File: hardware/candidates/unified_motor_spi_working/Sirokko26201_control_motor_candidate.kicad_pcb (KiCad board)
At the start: 2 copper layers, 180 x 170 mm, 112 parts, among them J1 DEVKITC1_J1, J10 TC_K_EXHAUST_T+_T-, J102 MOTOR_24V_HIGH_SPEED; 125W_HE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, J11 TC_K_AIR_T+_T-, J12 ROOM_DS18B20_HARNESS, J13 24V_LOGIC_INPUT_ONLY__DRAFT_N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, J22 PANEL_DRY_CONTACTS_3V3, J23 LOCAL_BUTTONS_3V3__SET_UP_DOW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, J24 RESET_HW_SPDT_BBM_3V3, J25 THERMAL_AND_HW_ENABLE_3V3_ONLY, J26 TFT_GMT020-02-7P_ST7789V_7P_S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, J3 DEVKITC1_J3, Q101 IRFB4110PBF (100V; RDS(on) @ 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, U1 TPS3431SDRBR, U10 MAX31856MUD+, U101 LM5013DDAR, U2 SN74HCS74D, U3 SN74HCS14D, U4 SN74HCS30D, U5 SN74HCS30D, U6 SN74HCS11D, U7 TPS3839G33DBZR, U8 SN74LVC1G14DBVR, U9 MAX31856MUD+, U9001 LTC7001IMSE#PBF; MSOP-10 EP, U9002 INA240A1ID, U9003 LMV331M5X/NOPB, U9004 SN74LVC1G32DBVR, U9005 SN74LVC1G08DBVR, U9006 SN74LVC1G08DBVR, U9007 LM317HVT/NOPB TO-220; TJ 0…12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

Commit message: hardware: WIP continue unified TFT routing 215-55
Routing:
- net /TFT_DC: track 0.00 -> 108.4 mm
- net /TFT_CS: track 0.00 -> 105.8 mm, vias 0 -> 1
- net /+3V3: track 72.6 -> 96.4 mm, vias 1 -> 2
- net /TFT_RESET_N: track 0.00 -> 8.82 mm, vias 0 -> 1
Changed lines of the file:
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@@
+	)
+	(segment
+		(start 21 74.975)
+		(end 24 74.975)
+		(width 0.4)
+		(layer "F.Cu")
+		(net "/+3V3")
 	)
 	(segment
@@
 	)
 	(segment
+		(start 24 74.975)
+		(end 24 87.7)
+		(width 0.4)
+		(layer "F.Cu")
+		(net "/+3V3")
+	)
+	(segment
 		(start 27.875 29.05)
 		(end 25 27.5)
@@
 	)
 	(via
+		(at 24 87.7)
+		(size 0.6)
+		(drill 0.3)
+		(layers "F.Cu" "B.Cu")
+		(net "/+3V3")
+	)
+	(via
 		(at 21.725 29.05)
 		(size 0.6)
@@
 		)
 		(filling no)
+		(net "/+3V3")
+	)
+	(segment
+		(start 24 87.7)
+		(end 16 87.7)
+		(width 0.4)
+		(layer "B.Cu")
 		(net "/+3V3")
 	)
@@
 	)
 	(segment
+		(start 19.5 76.625)
+		(end 21 76.625)
+		(width 0.25)
+		(layer "F.Cu")
+		(net "/TFT_CS")
+	)
+	(segment
+		(start 20 94)
+		(end 79.8 94)
+		(width 0.25)
+		(layer "F.Cu")
+		(net "/TFT_CS")
+	)
+	(segment
+		(start 20 77.625)
+		(end 20 94)
+		(width 0.25)
+		(layer "F.Cu")
+		(net "/TFT_CS")
+	)
+	(segment
+		(start 21 76.625)
+		(end 20 77.625)
+		(width 0.25)
+		(layer "F.Cu")
+		(net "/TFT_CS")
+	)
+	(segment
+		(start 16 75)
+		(end 19.5 75)
+		(width 0.25)
+		(layer "F.Cu")
+		(net "/TFT_CS")
+	)
+	(segment
+		(start 19.5 75)
+		(end 19.5 76.625)
+		(width 0.25)
+		(layer "F.Cu")
+		(net "/TFT_CS")
+	)
+	(segment
+		(start 79.8 94)
+		(end 79.8 75.64)
+		(width 0.25)
+		(layer "F.Cu")
+		(net "/TFT_CS")
+	)
+	(via
+		(at 79.8 75.64)
+		(size 0.6)
+		(drill 0.3)
+		(layers "F.Cu" "B.Cu")
+		(net "/TFT_CS")
+	)
+	(segment
+		(start 79.8 75.64)
+		(end 83 75.64)
+		(width 0.25)
+		(layer "B.Cu")
+		(net "/TFT_CS")
+	)
+	(segment
 		(start 120.825 68)
 		(end 125 68.825)
@@
 	)
 	(segment
+		(start 22.5 80.075)
+		(end 22.5 79.5)
+		(width 0.25)
+		(layer "F.Cu")
+		(net "/TFT_RESET_N")
+	)
+	(segment
+		(start 21 80.075)
+		(end 22.5 80.075)
+		(width 0.25)
+		(layer "F.Cu")
+		(net "/TFT_RESET_N")
+	)
+	(via
+		(at 22.5 79.5)
+		(size 0.6)
+		(drill 0.3)
+		(layers "F.Cu" "B.Cu")
+		(net "/TFT_RESET_N")
+	)
+	(segment
+		(start 18.42 80.08)
+		(end 16 80.08)
+		(width 0.25)
+		(layer "B.Cu")
+		(net "/TFT_RESET_N")
+	)
+	(segment
+		(start 22.5 79.5)
+		(end 19 79.5)
+		(width 0.25)
+		(layer "B.Cu")
+		(net "/TFT_RESET_N")
+	)
+	(segment
+		(start 19 79.5)
+		(end 18.42 80.08)
+		(width 0.25)
+		(layer "B.Cu")
+		(net "/TFT_RESET_N")
+	)
+	(segment
 		(start 63.5 26.5)
 		(end 59.725 26.5)
@@
 		(net "/TC_EXH_DRDY")
 	)
+	(segment
+		(start 18 96)
+		(end 81.5 96)
+		(width 0.25)
+		(layer "F.Cu")
+		(net "/TFT_DC")
+	)
+	(segment
+		(start 18 77.54)
+		(end 18 96)
+		(width 0.25)
+		(layer "F.Cu")
+		(net "/TFT_DC")
+	)
+	(segment
+		(start 81.5 73.1)
+		(end 83 73.1)
+		(width 0.25)
+		(layer "F.Cu")
+		(net "/TFT_DC")
+	)
+	(segment
+		(start 16 77.54)
+		(end 18 77.54)
+		(width 0.25)
+		(layer "F.Cu")
+		(net "/TFT_DC")
+	)
+	(segment
+		(start 81.5 96)
+		(end 81.5 73.1)
+		(width 0.25)
+		(layer "F.Cu")
+		(net "/TFT_DC")
+	)
 	(zone

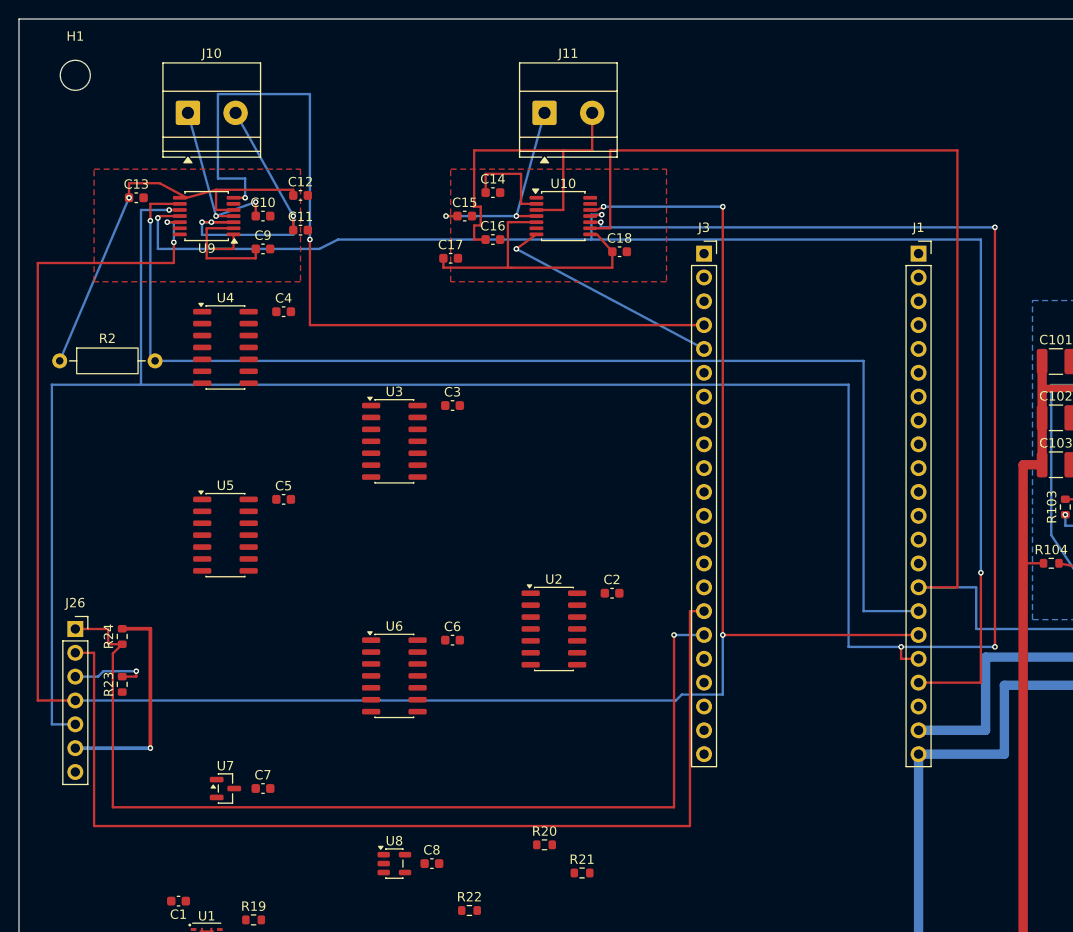
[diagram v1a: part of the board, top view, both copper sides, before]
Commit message: hardware: WIP route unified TFT power ground and EN 251-72
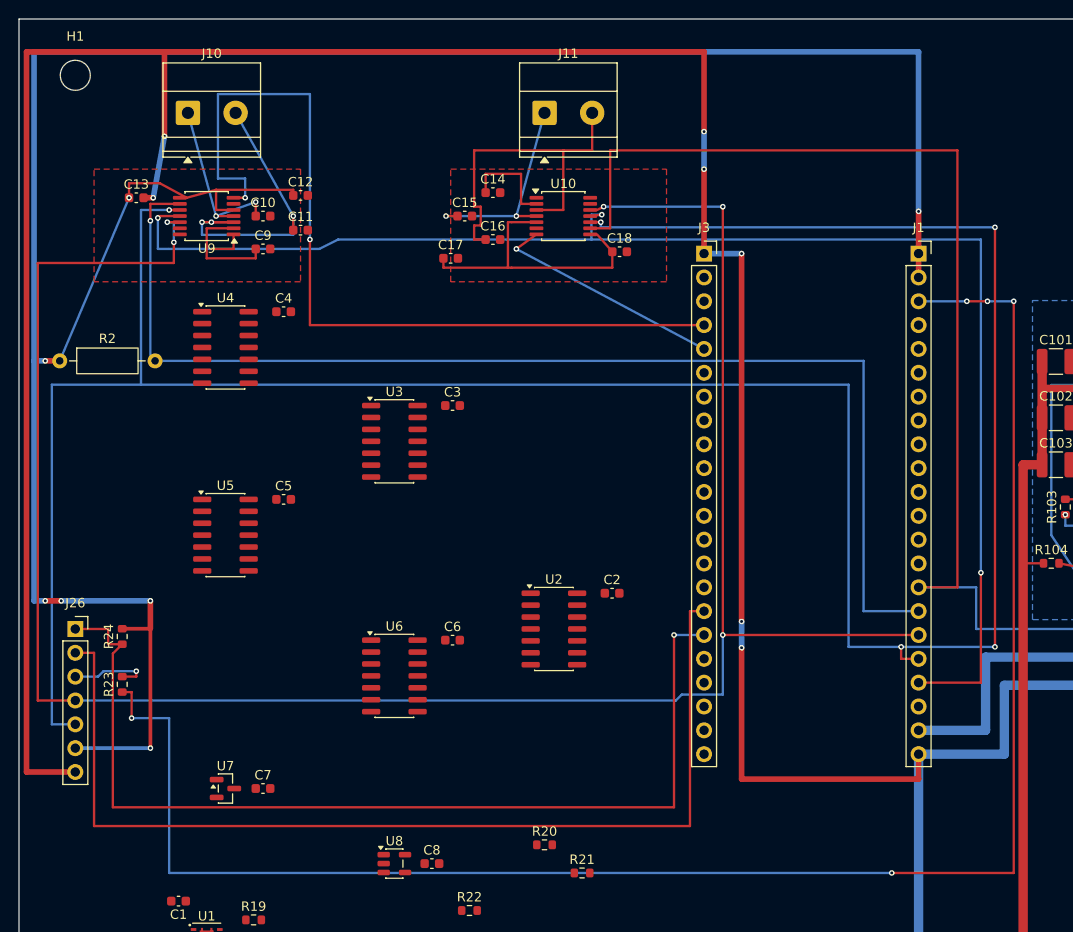
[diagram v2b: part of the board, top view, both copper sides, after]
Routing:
- net /GND: track 226.1 -> 500.0 mm, vias 9 -> 16
- net /+3V3: track 96.4 -> 291.3 mm, vias 2 -> 7
- net /EN_CHIP_PU: track 0.00 -> 185.3 mm, vias 0 -> 5

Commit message: hardware: WIP publish U4/U5 logic supply routing 283/72
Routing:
- net /+3V3: track 291.3 -> 385.4 mm
- net /GND: track 500.0 -> 571.2 mm
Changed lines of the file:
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@@
+	)
+	(segment
+		(start 36 61.19)
+		(end 36 65)
+		(width 0.4)
+		(layer "F.Cu")
+		(net "/+3V3")
+	)
+	(segment
+		(start 36 59)
+		(end 36 61.19)
+		(width 0.4)
+		(layer "F.Cu")
+		(net "/+3V3")
 	)
 	(segment
@@
 	)
 	(segment
+		(start 34.475 41.19)
+		(end 37.425 41.19)
+		(width 0.4)
+		(layer "F.Cu")
+		(net "/+3V3")
+	)
+	(segment
 		(start 62.1 31.65)
 		(end 62.1 36.5)
@@
 	)
 	(segment
+		(start 27 59)
+		(end 27 67.54)
+		(width 0.25)
+		(layer "F.Cu")
+		(net "/+3V3")
+	)
+	(segment
 		(start 31 30.35)
 		(end 31 28.2)
@@
 	)
 	(segment
+		(start 18 42.77)
+		(end 18 39)
+		(width 0.4)
+		(layer "F.Cu")
+		(net "/+3V3")
+	)
+	(segment
+		(start 34.475 63.73)
+		(end 36 63.73)
+		(width 0.25)
+		(layer "F.Cu")
+		(net "/+3V3")
+	)
+	(segment
+		(start 14.34 46.43)
+		(end 18 50.09)
+		(width 0.4)
+		(layer "F.Cu")
+		(net "/+3V3")
+	)
+	(segment
 		(start 55.225 36.5)
 		(end 55.225 35.5)
@@
 	)
 	(segment
+		(start 18 50.09)
+		(end 18 59)
+		(width 0.4)
+		(layer "F.Cu")
+		(net "/+3V3")
+	)
+	(segment
 		(start 31 28.2)
 		(end 39.225 28.2)
@@
 	)
 	(segment
+		(start 34.475 43.73)
+		(end 36 43.73)
+		(width 0.25)
+		(layer "F.Cu")
+		(net "/+3V3")
+	)
+	(segment
 		(start 73.225 36.5)
 		(end 73.225 34.8)
@@
 	)
 	(segment
+		(start 14.34 46.43)
+		(end 18 42.77)
+		(width 0.4)
+		(layer "F.Cu")
+		(net "/+3V3")
+	)
+	(segment
+		(start 27 67.54)
+		(end 29.525 67.54)
+		(width 0.25)
+		(layer "F.Cu")
+		(net "/+3V3")
+	)
+	(segment
 		(start 105.86 30.5)
 		(end 105.86 35)
@@
 	)
 	(segment
+		(start 36 41.19)
+		(end 36 45)
+		(width 0.4)
+		(layer "F.Cu")
+		(net "/+3V3")
+	)
+	(segment
+		(start 34.475 65)
+		(end 36 65)
+		(width 0.25)
+		(layer "F.Cu")
+		(net "/+3V3")
+	)
+	(segment
+		(start 34.475 61.19)
+		(end 37.425 61.19)
+		(width 0.4)
+		(layer "F.Cu")
+		(net "/+3V3")
+	)
+	(segment
 		(start 14.5 72)
 		(end 12.8 72)
@@
 	)
 	(segment
+		(start 36 39)
+		(end 36 41.19)
+		(width 0.4)
+		(layer "F.Cu")
+		(net "/+3V3")
+	)
+	(segment
+		(start 18 59)
+		(end 36 59)
+		(width 0.4)
+		(layer "F.Cu")
+		(net "/+3V3")
+	)
+	(segment
 		(start 64.4 31.65)
 		(end 62.5 31.65)
@@
 	)
 	(segment
+		(start 34.475 45)
+		(end 36 45)
+		(width 0.25)
+		(layer "F.Cu")
+		(net "/+3V3")
+	)
+	(segment
 		(start 62.5 36.5)
 		(end 73.225 36.5)
 		(width 0.25)
+		(layer "F.Cu")
+		(net "/+3V3")
+	)
+	(segment
+		(start 18 39)
+		(end 36 39)
+		(width 0.4)
 		(layer "F.Cu")
 		(net "/+3V3")
@@
 	)
 	(segment
+		(start 38.975 61.19)
+		(end 39.7 60.465)
+		(width 0.4)
+		(layer "F.Cu")
+		(net "/GND")
+	)
+	(segment
 		(start 10.8 13.5)
 		(end 83 13.5)
 		(width 0.6)
+		(layer "F.Cu")
+		(net "/GND")
+	)
+	(segment
+		(start 39.7 50.3)
+		(end 39.7 40.465)
+		(width 0.4)
+		(layer "F.Cu")
+		(net "/GND")
+	)
+	(segment
+		(start 29.525 48.81)
+		(end 28.2 48.81)
+		(width 0.4)
 		(layer "F.Cu")
 		(net "/GND")
@@
 	)
 	(segment
+		(start 28.2 70.3)
+		(end 39.7 70.3)
+		(width 0.4)
+		(layer "F.Cu")
+		(net "/GND")
+	)
+	(segment
 		(start 121.975 46.5)
 		(end 123.5 46.5)
@@
 	)
 	(segment
+		(start 39.7 38)
+		(end 36.775 35.075)
+		(width 0.4)
+		(layer "F.Cu")
+		(net "/GND")
+	)
+	(segment
 		(start 121.975 52.5)
 		(end 123.5 52.5)
@@
 	)
 	(segment
+		(start 28.2 68.81)
+		(end 28.2 70.3)
+		(width 0.4)
+		(layer "F.Cu")
+		(net "/GND")
+	)
+	(segment
+		(start 29.525 68.81)
+		(end 28.2 68.81)
+		(width 0.4)
+		(layer "F.Cu")
+		(net "/GND")
+	)
+	(segment
 		(start 168 43.525)
 		(end 173 43.525)
@@
 	)
 	(segment
+		(start 39.7 70.3)
+		(end 39.7 60.465)
+		(width 0.4)
+		(layer "F.Cu")
+		(net "/GND")
+	)
+	(segment
 		(start 121.975 57.5)
 		(end 123.5 57.5)
@@
 	)
 	(segment
+		(start 28.2 48.81)
+		(end 28.2 50.3)
+		(width 0.4)
+		(layer "F.Cu")
+		(net "/GND")
+	)
+	(segment
 		(start 125.3 48.095)
 		(end 128 48.095)
@@
 	)
 	(segment
+		(start 38.975 41.19)
+		(end 39.7 40.465)
+		(width 0.4)
+		(layer "F.Cu")
+		(net "/GND")
+	)
+	(segment
 		(start 16 90.24)
 		(end 10.8 90.24)
@@
 		(end 83 22)
 		(width 0.6)
+		(layer "F.Cu")
+		(net "/GND")
+	)
+	(segment
+		(start 39.7 60.465)
+		(end 39.7 50.3)
+		(width 0.4)
 		(layer "F.Cu")
 		(net "/GND")
@@
 	)
 	(segment
+		(start 28.2 50.3)
+		(end 39.7 50.3)
+		(width 0.4)
+		(layer "F.Cu")
+		(net "/GND")
+	)
+	(segment
 		(start 121.5 61.175)
 		(end 122.7 61.175)
@@
 		(layer "F.Cu")
 		(net "/GND")
+	)
+	(segment
+		(start 36.775 35.075)
+		(end 36.775 31)
+		(width 0.4)
+		(layer "F.Cu")
+		(net "/GND")
+	)
+	(segment
+		(start 39.7 40.465)
+		(end 39.7 38)
+		(width 0.4)
+		(layer "F.Cu")
+		(net "/GND")

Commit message: hardware: WIP publish U3/C3 supply 294/74 and RESET erratum
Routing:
- net /GND: track 571.2 -> 605.7 mm
- net /+3V3: track 385.4 -> 413.9 mm, vias 7 -> 9
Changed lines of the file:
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@@
+	)
+	(segment
+		(start 42 45)
+		(end 42 49)
+		(width 0.4)
+		(layer "F.Cu")
+		(net "/+3V3")
 	)
 	(segment
@@
 	)
 	(segment
+		(start 55.425 49)
+		(end 55.425 51.19)
+		(width 0.4)
+		(layer "F.Cu")
+		(net "/+3V3")
+	)
+	(segment
+		(start 36 45)
+		(end 38 45)
+		(width 0.4)
+		(layer "F.Cu")
+		(net "/+3V3")
+	)
+	(segment
 		(start 62.5 31.65)
 		(end 62.1 31.65)
@@
 	)
 	(segment
+		(start 42 49)
+		(end 55.425 49)
+		(width 0.4)
+		(layer "F.Cu")
+		(net "/+3V3")
+	)
+	(segment
 		(start 27.875 29.05)
 		(end 31 28.2)
@@
 		(start 34.475 61.19)
 		(end 37.425 61.19)
+		(width 0.4)
+		(layer "F.Cu")
+		(net "/+3V3")
+	)
+	(segment
+		(start 52.475 51.19)
+		(end 55.425 51.19)
 		(width 0.4)
 		(layer "F.Cu")
@@
 	)
 	(via
+		(at 42 45)
+		(size 0.6)
+		(drill 0.3)
+		(layers "F.Cu" "B.Cu")
+		(net "/+3V3")
+	)
+	(via
+		(at 38 45)
+		(size 0.6)
+		(drill 0.3)
+		(layers "F.Cu" "B.Cu")
+		(net "/+3V3")
+	)
+	(via
 		(at 24 72)
 		(size 0.6)
@@
 		(end 14.5 72)
 		(width 0.6)
+		(layer "B.Cu")
+		(net "/+3V3")
+	)
+	(segment
+		(start 38 45)
+		(end 42 45)
+		(width 0.4)
 		(layer "B.Cu")
 		(net "/+3V3")
@@
 	)
 	(segment
+		(start 56.975 51.19)
+		(end 56.975 43.5)
+		(width 0.4)
+		(layer "F.Cu")
+		(net "/GND")
+	)
+	(segment
 		(start 28.2 70.3)
 		(end 39.7 70.3)
+		(width 0.4)
+		(layer "F.Cu")
+		(net "/GND")
+	)
+	(segment
+		(start 47.525 58.81)
+		(end 45.5 58.81)
 		(width 0.4)
 		(layer "F.Cu")
@@
 	)
 	(segment
+		(start 45.5 60.5)
+		(end 39.7 60.5)
+		(width 0.4)
+		(layer "F.Cu")
+		(net "/GND")
+	)
+	(segment
 		(start 87 35)
 		(end 87 74.2)
@@
 	)
 	(segment
+		(start 56.975 43.5)
+		(end 39.7 43.5)
+		(width 0.4)
+		(layer "F.Cu")
+		(net "/GND")
+	)
+	(segment
 		(start 36.775 35.075)
 		(end 36.775 31)
@@
 		(layer "F.Cu")
 		(net "/GND")
+	)
+	(segment
+		(start 45.5 58.81)
+		(end 45.5 60.5)
+		(width 0.4)
+		(layer "F.Cu")
+		(net "/GND")

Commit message: hardware: WIP publish U2/C2 supply routing 313/74
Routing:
- net /GND: track 605.7 -> 682.3 mm
- net /+3V3: track 413.9 -> 457.2 mm
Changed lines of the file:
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@@
+	)
+	(segment
+		(start 62.5 75)
+		(end 62.5 69)
+		(width 0.4)
+		(layer "F.Cu")
+		(net "/+3V3")
 	)
 	(segment
@@
 	)
 	(segment
+		(start 69.475 69)
+		(end 69.475 71.19)
+		(width 0.4)
+		(layer "F.Cu")
+		(net "/+3V3")
+	)
+	(segment
+		(start 64.525 75)
+		(end 62.5 75)
+		(width 0.4)
+		(layer "F.Cu")
+		(net "/+3V3")
+	)
+	(segment
 		(start 32.125 30.35)
 		(end 31 30.35)
@@
 	)
 	(segment
+		(start 58.425 69)
+		(end 69.475 69)
+		(width 0.4)
+		(layer "F.Cu")
+		(net "/+3V3")
+	)
+	(segment
 		(start 27 59)
 		(end 27 67.54)
@@
 	)
 	(segment
+		(start 55.425 51.19)
+		(end 55.425 66)
+		(width 0.4)
+		(layer "F.Cu")
+		(net "/+3V3")
+	)
+	(segment
 		(start 31 30.35)
 		(end 31 28.2)
@@
 	)
 	(segment
+		(start 69.475 71.19)
+		(end 72.425 71.19)
+		(width 0.4)
+		(layer "F.Cu")
+		(net "/+3V3")
+	)
+	(segment
 		(start 39.225 28.2)
 		(end 39.225 28.8)
@@
 		(end 12.8 72)
 		(width 0.6)
+		(layer "F.Cu")
+		(net "/+3V3")
+	)
+	(segment
+		(start 55.425 66)
+		(end 58.425 69)
+		(width 0.4)
 		(layer "F.Cu")
 		(net "/+3V3")
@@
 	)
 	(segment
+		(start 56.975 51.19)
+		(end 58 52.215)
+		(width 0.4)
+		(layer "F.Cu")
+		(net "/GND")
+	)
+	(segment
 		(start 39.7 50.3)
 		(end 39.7 40.465)
@@
 	)
 	(segment
+		(start 78 79.8)
+		(end 71 79.8)
+		(width 0.4)
+		(layer "F.Cu")
+		(net "/GND")
+	)
+	(segment
+		(start 58 64)
+		(end 78 64)
+		(width 0.4)
+		(layer "F.Cu")
+		(net "/GND")
+	)
+	(segment
+		(start 58 52.215)
+		(end 58 64)
+		(width 0.4)
+		(layer "F.Cu")
+		(net "/GND")
+	)
+	(segment
 		(start 25.5 13.5)
 		(end 25.5 22.5)
@@
 		(end 105.86 88.34)
 		(width 0.6)
+		(layer "F.Cu")
+		(net "/GND")
+	)
+	(segment
+		(start 78 71.19)
+		(end 73.975 71.19)
+		(width 0.4)
 		(layer "F.Cu")
 		(net "/GND")
@@
 	)
 	(segment
+		(start 78 64)
+		(end 78 79.8)
+		(width 0.4)
+		(layer "F.Cu")
+		(net "/GND")
+	)
+	(segment
 		(start 28.2 70.3)
 		(end 39.7 70.3)
+		(width 0.4)
+		(layer "F.Cu")
+		(net "/GND")
+	)
+	(segment
+		(start 64.525 79.8)
+		(end 64.525 78.81)
 		(width 0.4)
 		(layer "F.Cu")
@@
 	)
 	(segment
+		(start 71 75)
+		(end 69.475 75)
+		(width 0.4)
+		(layer "F.Cu")
+		(net "/GND")
+	)
+	(segment
 		(start 87 91)
 		(end 105.86 91)
@@
 	)
 	(segment
+		(start 71 79.8)
+		(end 71 75)
+		(width 0.4)
+		(layer "F.Cu")
+		(net "/GND")
+	)
+	(segment
 		(start 83 26)
 		(end 83 35)
@@
 		(start 29.525 68.81)
 		(end 28.2 68.81)
+		(width 0.4)
+		(layer "F.Cu")
+		(net "/GND")
+	)
+	(segment
+		(start 71 73.73)
+		(end 69.475 73.73)
 		(width 0.4)
 		(layer "F.Cu")
@@
 		(layer "F.Cu")
 		(net "/GND")
+	)
+	(segment
+		(start 71 79.8)
+		(end 64.525 79.8)
+		(width 0.4)
+		(layer "F.Cu")
+		(net "/GND")
+	)
+	(segment
+		(start 71 75)
+		(end 71 73.73)
+		(width 0.4)
+		(layer "F.Cu")
+		(net "/GND")

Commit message: hardware: WIP publish protection logic signals 326/78
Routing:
- net /NOT_RESET_ACCEPT: track 0.00 -> 40.4 mm, vias 0 -> 2
- net /NOT_CLEAR_OK: track 0.00 -> 27.8 mm, vias 0 -> 2
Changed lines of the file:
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@@
+	)
+	(segment
+		(start 35 48.81)
+		(end 35 49.6)
+		(width 0.25)
+		(layer "F.Cu")
+		(net "/NOT_CLEAR_OK")
+	)
+	(segment
+		(start 53.8 55)
+		(end 52.475 55)
+		(width 0.25)
+		(layer "F.Cu")
+		(net "/NOT_CLEAR_OK")
+	)
+	(segment
+		(start 34.475 48.81)
+		(end 35 48.81)
+		(width 0.25)
+		(layer "F.Cu")
+		(net "/NOT_CLEAR_OK")
+	)
+	(via
+		(at 53.8 55)
+		(size 0.6)
+		(drill 0.3)
+		(layers "F.Cu" "B.Cu")
+		(net "/NOT_CLEAR_OK")
+	)
+	(via
+		(at 35 49.6)
+		(size 0.6)
+		(drill 0.3)
+		(layers "F.Cu" "B.Cu")
+		(net "/NOT_CLEAR_OK")
+	)
+	(segment
+		(start 35 49.6)
+		(end 35 54)
+		(width 0.25)
+		(layer "B.Cu")
+		(net "/NOT_CLEAR_OK")
+	)
+	(segment
+		(start 35 54)
+		(end 37.1 56.1)
+		(width 0.25)
+		(layer "B.Cu")
+		(net "/NOT_CLEAR_OK")
+	)
+	(segment
+		(start 53.8 56.1)
+		(end 53.8 55)
+		(width 0.25)
+		(layer "B.Cu")
+		(net "/NOT_CLEAR_OK")
+	)
+	(segment
+		(start 37.1 56.1)
+		(end 53.8 56.1)
+		(width 0.25)
+		(layer "B.Cu")
+		(net "/NOT_CLEAR_OK")
+	)
+	(segment
+		(start 35.9 68.81)
+		(end 34.475 68.81)
+		(width 0.25)
+		(layer "F.Cu")
+		(net "/NOT_RESET_ACCEPT")
+	)
+	(segment
+		(start 52.475 52.46)
+		(end 53.8 52.46)
+		(width 0.25)
+		(layer "F.Cu")
+		(net "/NOT_RESET_ACCEPT")
+	)
+	(via
+		(at 53.8 52.46)
+		(size 0.6)
+		(drill 0.3)
+		(layers "F.Cu" "B.Cu")
+		(net "/NOT_RESET_ACCEPT")
+	)
+	(via
+		(at 35.9 68.81)
+		(size 0.6)
+		(drill 0.3)
+		(layers "F.Cu" "B.Cu")
+		(net "/NOT_RESET_ACCEPT")
+	)
+	(segment
+		(start 54.8 69.81)
+		(end 36.9 69.81)
+		(width 0.25)
+		(layer "B.Cu")
+		(net "/NOT_RESET_ACCEPT")
+	)
+	(segment
+		(start 53.8 52.46)
+		(end 54.8 52.46)
+		(width 0.25)
+		(layer "B.Cu")
+		(net "/NOT_RESET_ACCEPT")
+	)
+	(segment
+		(start 36.9 69.81)
+		(end 35.9 68.81)
+		(width 0.25)
+		(layer "B.Cu")
+		(net "/NOT_RESET_ACCEPT")
+	)
+	(segment
+		(start 54.8 52.46)
+		(end 54.8 69.81)
+		(width 0.25)
+		(layer "B.Cu")
+		(net "/NOT_RESET_ACCEPT")
 	)
 	(segment

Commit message: hardware: WIP restore R9001 FPID and confirm nominal land pattern
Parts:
- R9001: footprint WSLP2726 -> Sirokko_Power:WSLP2726
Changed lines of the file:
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@@
 		)
 	)
-	(footprint "WSLP2726"
+	(footprint "Sirokko_Power:WSLP2726"
 		(layer "F.Cu")
 		(at 160 145 -90)
